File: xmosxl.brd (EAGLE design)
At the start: 130 x 85 mm, 145 parts, among them IC1 74LVC1T45W6-7, IC2 74LVC1T45W6-7, IC3 74LVC1T45W6-7, IC4 74LVC1T45W6-7, IC5 74LVC1T45W6-7, IC6 74ALVC164245DGG_11, IC7 74ALVC164245DGG_11, IC8 74LVC1T45W6-7, IC9 74LVC1T45W6-7, U1 24 MHz Osc. (F535L-24)

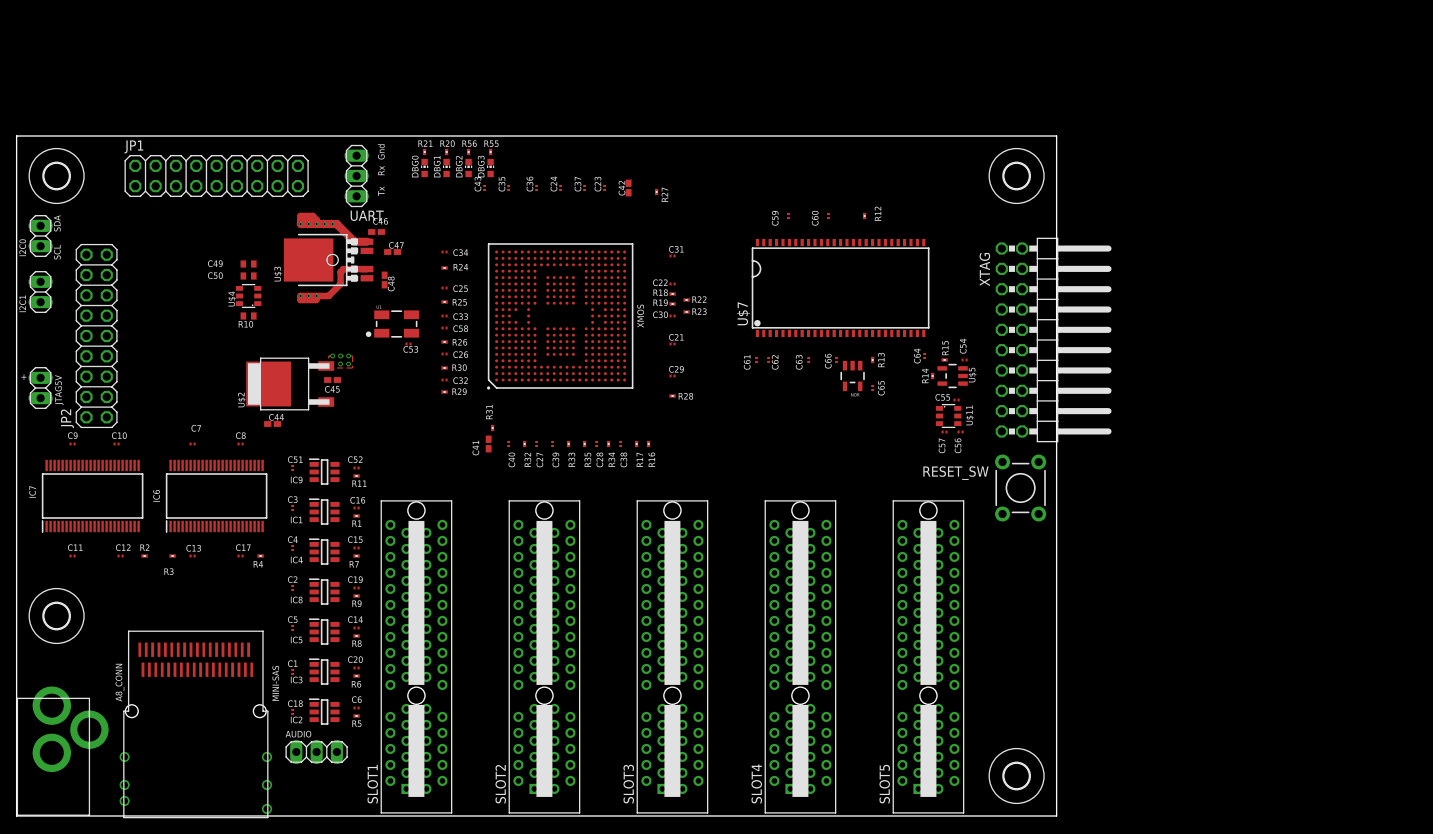
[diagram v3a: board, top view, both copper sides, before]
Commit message: Start reconfiguring for STM
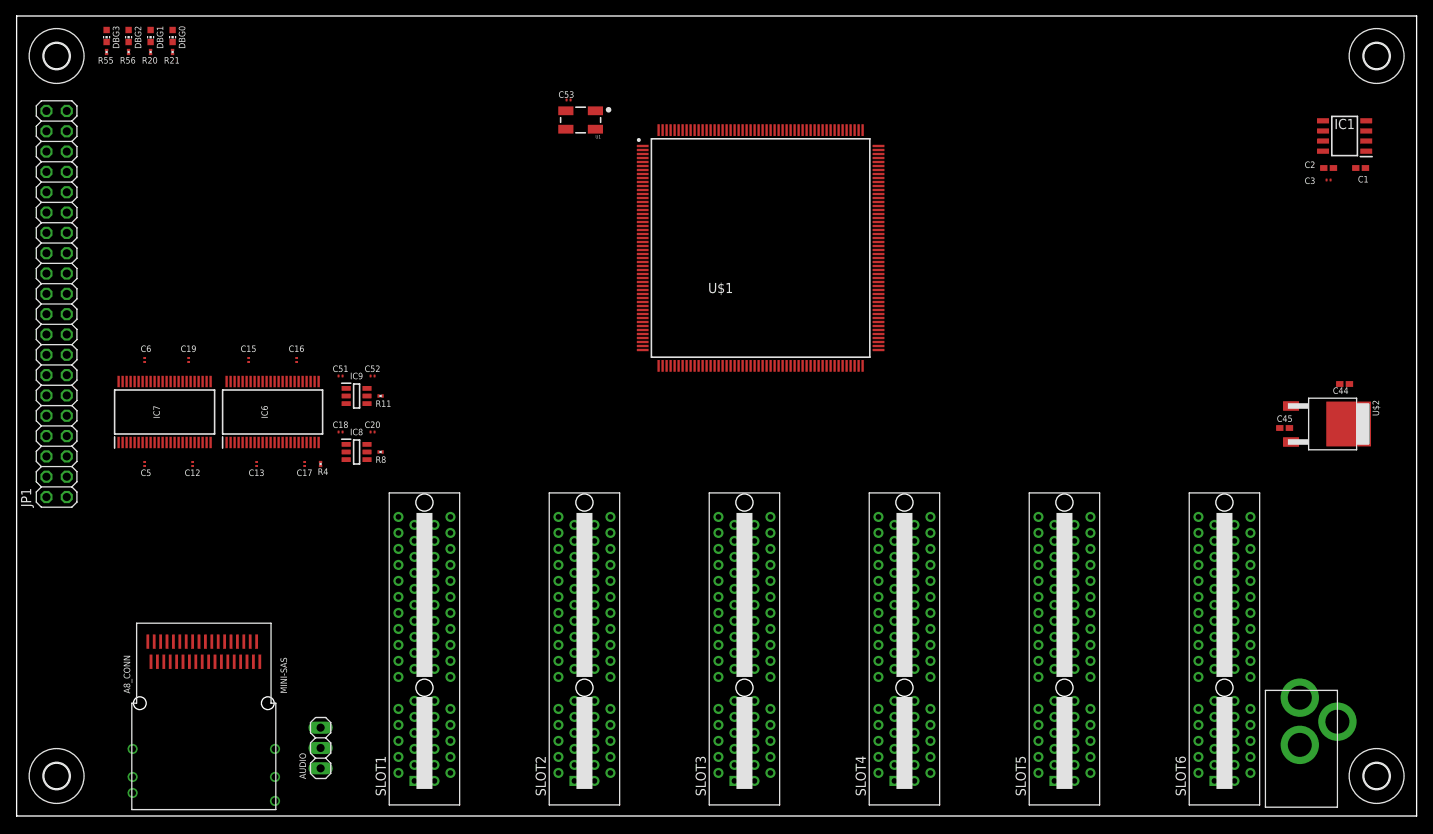
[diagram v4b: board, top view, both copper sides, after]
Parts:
- removed C10, C11, C14, C21, C22, C23, C24, C25, C26, C27, C28, C29, C30, C31, C32, C33, C34, C35, C36, C37, C38, C39, C4, C40, C43, C54, C55, C58, C7, C8, C9: 0.1uF, rcl:C0201
- removed C41, C42, C47: 10uF, rcl:C0402K
- removed C46, C48: 1uF, rcl:C0402K
- removed C49: 0.1uF, rcl:C0402
- removed C50: 120pF, rcl:C0402
- removed C56: 120pF, rcl:C0201
- removed C57: 10nF, rcl:C0201
- removed C59, C60, C61, C62, C63, C64, C65, C66: 100nF, rcl:C0201
- removed I2C0, I2C1: (no value), pinhead:1X02
- removed IC2, IC3, IC4, IC5: 74LVC1T45W6-7, samacsys:SOT95P285X140-6N
- removed JP2: (no value), pinhead:2X09
- removed JTAG5V: PSU, pinhead:1X02
- removed NOR: SN74LVC1G02, sjg-logic:SOT23-5
- removed R1, R12, R13, R18, R19, R2, R22, R23, R25, R26, R3, R5, R6, R7, R9: 10K, rcl:R0201
- removed R10: 47K, rcl:R0402
- removed R14, R15: 47K, rcl:R0201
- removed R16, R17, R31, R32, R33, R34, R35: 33R, rcl:R0201
- removed R24: 2.2R, rcl:R0201
- removed R27, R28: 43R2, rcl:R0201
- removed R29, R30: 4K7, rcl:R0201
- removed RESET_SW: MANUAL_RESET, SparkFun:TACTILE-PTH
- removed U$11: TPS3808G09DBVR, sjg-power:SOT23-6
- removed U$3: LD49300, sjg-power:TO252-51
- removed U$4: TPS3808G33DBVR, sjg-power:SOT23-6
- removed U$5: 74LVC1G07SE-7, sjg-logic:SOT23-5
- removed U$7: W9852G6KH, sjg-sdram:TSOP54-400
- removed UART: (no value), pinhead:1X03
- removed XMOS: XEF232, xmosxl:BGA374C80P21X21_1800X1800X136
- removed XTAG: 1175-1618-ND, pinhead:2X10/90
- added SLOT6: PCIE_64, pcie:PCI-E_64
- added U$1: STM32F767, xmosxl:QFP50P3000X3000X160-208N
- C1, C2: value 0.1uF -> 10uF; device rcl:C0201 -> rcl:C0402K
- C3: value 0.1uF -> 1uF
- IC1: value 74LVC1T45W6-7 -> MCP1727-1802E_SN; device samacsys:SOT95P285X140-6N -> samacsys:SOIC127P600X175-8N
- JP1: device pinhead:2X09 -> pinhead:2X20
- moved PJ-102AH 156.0 mm to (160.5, 5.50)
- moved C1 147.6 mm to (168.0, 81.0), turned to 180 degrees
- moved C2 139.7 mm to (164.0, 81.0), turned to 0 degrees
- moved IC1 135.9 mm to (166.0, 85.0), turned to 180 degrees
- moved C3 135.8 mm to (164.0, 79.5), turned to 0 degrees
- moved U$2 135.1 mm to (166.5, 49.0), turned to 270 degrees
- moved C44 134.1 mm to (166.0, 54.0), turned to 180 degrees
- moved C45 119.2 mm to (158.5, 48.5), turned to 180 degrees
- moved C6 50.9 mm to (16.0, 57.0), turned to 90 degrees
- moved DBG3 50.8 mm to (11.2, 97.5), turned to 180 degrees
- moved R55 49.6 mm to (11.2, 95.5), turned to 90 degrees
- moved H3 47.4 mm to (170.0, 95.0)
- moved DBG2 45.6 mm to (14.0, 97.5), turned to 180 degrees
- moved H4 45.0 mm to (170.0, 5.00)
- moved R56 44.3 mm to (14.0, 95.5), turned to 90 degrees
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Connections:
- removed net !DEBUG!: XMOS.D9, XTAG.11
- removed net !HALT!_DIR: IC4.5, R7.1, XMOS.C14
- removed net !IRQ!: IC3.4, XMOS.B21
- removed net !IRQ!_DIR: IC3.5, R6.1, XMOS.D14
- removed net !REF!_DIR: IC8.5, R9.1, XMOS.A15
- removed net !RESET!: R15.1, U$11.1, U$5.4, XMOS.B12, XMOS.C12
- removed net !RST!_DIR: IC2.5, R5.1, XMOS.B16
- removed net !SD_CAS!: NOR.1, U$7.17, XMOS.Y18
- removed net !SD_RAS!: U$7.18, XMOS.Y13
- removed net !SD_WE!: NOR.2, U$7.16, XMOS.AA18
- removed net A_DIR: IC7.1, IC7.24, R2.1, XMOS.B15
- removed net D_DIR: IC6.1, R3.1, XMOS.A14
- removed net EN_1V0: R10.1, U$3.1, U$4.1
- removed net JTAG_DN0: XMOS.U1, XTAG.14
- removed net JTAG_DN1: XMOS.U2, XTAG.18
- removed net JTAG_UP0: R16.2, XTAG.10
- removed net JTAG_UP1: R17.2, XTAG.6
- removed net N$1: R14.1, U$5.2, XTAG.15
- removed net N$10: R26.2, XMOS.D10
- removed net N$11: R27.2, XMOS.W16
- removed net N$12: R28.2, XMOS.W6
- removed net N$13: UART.2, XMOS.E3
- removed net N$14: NOR.4, U$7.15, U$7.39
- removed net N$15: R12.2, U$7.37
- removed net N$17: R13.2, U$7.19
- removed net N$20: UART.1, XMOS.D3
- removed net N$22: R16.1, XMOS.V2
- removed net N$23: R17.1, XMOS.V1
- removed net N$27: R31.1, XMOS.N2
- removed net N$28: R32.1, XMOS.P2
- removed net N$29: R34.1, XMOS.R1
- removed net N$30: R35.1, XMOS.R2
- removed net N$38: JTAG5V.2, XTAG.1
- removed net N$5: C50.1, U$4.4
- removed net N$6: C56.1, U$11.4
- removed net N$7: C58.1, R24.2, XMOS.F11
- removed net N$8: R14.2, U$5.5
- removed net N$9: R25.1, XMOS.C10
- removed net R/!W!_DIR: IC1.5, R1.1, XMOS.D15
- removed net RD4: IC6.35, XMOS.W18
- removed net RD5: IC6.36, XMOS.V18
- removed net RX0: JP1.1, XMOS.N1
- removed net RX1: JP1.5, XMOS.M1
- removed net RX2: JP1.9, XMOS.M2
- removed net RX3: JP1.13, XMOS.M3
- removed net RX4: JP1.17, R33.1, XMOS.L3, XMOS.P1
- removed net SBUS_A0: SLOT1.A3, SLOT2.A3, SLOT3.A3, SLOT4.A3, SLOT5.A3, XMOS.A5
- removed net SBUS_A1: SLOT1.A4, SLOT2.A4, SLOT3.A4, SLOT4.A4, SLOT5.A4, XMOS.B5
- removed net SBUS_A10: SLOT1.A13, SLOT2.A13, SLOT3.A13, SLOT4.A13, SLOT5.A13, XMOS.T1
- removed net SBUS_A11: SLOT1.A14, SLOT2.A14, SLOT3.A14, SLOT4.A14, SLOT5.A14, XMOS.U3
- removed net SBUS_A12: SLOT1.A15, SLOT2.A15, SLOT3.A15, SLOT4.A15, SLOT5.A15, XMOS.B7
- removed net SBUS_A13: SLOT1.A16, SLOT2.A16, SLOT3.A16, SLOT4.A16, SLOT5.A16, XMOS.A7
- removed net SBUS_A14: SLOT1.A17, SLOT2.A17, SLOT3.A17, SLOT4.A17, SLOT5.A17, XMOS.B6
- removed net SBUS_A15: SLOT1.A18, SLOT2.A18, SLOT3.A18, SLOT4.A18, SLOT5.A18, XMOS.C6
- removed net SBUS_A2: SLOT1.A5, SLOT2.A5, SLOT3.A5, SLOT4.A5, SLOT5.A5, XMOS.C5
- removed net SBUS_A3: SLOT1.A6, SLOT2.A6, SLOT3.A6, SLOT4.A6, SLOT5.A6, XMOS.D5
- removed net SBUS_A4: SLOT1.A7, SLOT2.A7, SLOT3.A7, SLOT4.A7, SLOT5.A7, XMOS.C4
- removed net SBUS_A5: SLOT1.A8, SLOT2.A8, SLOT3.A8, SLOT4.A8, SLOT5.A8, XMOS.D4
- removed net SBUS_A6: SLOT1.A9, SLOT2.A9, SLOT3.A9, SLOT4.A9, SLOT5.A9, XMOS.A4
- removed net SBUS_A7: SLOT1.A10, SLOT2.A10, SLOT3.A10, SLOT4.A10, SLOT5.A10, XMOS.B4
- removed net SBUS_A8: SLOT1.A11, SLOT2.A11, SLOT3.A11, SLOT4.A11, SLOT5.A11, XMOS.F1
- removed net SBUS_A9: SLOT1.A12, SLOT2.A12, SLOT3.A12, SLOT4.A12, SLOT5.A12, XMOS.R3
- removed net SBUS_CLK: SLOT1.A19, SLOT2.A19, SLOT3.A19, SLOT4.A19, SLOT5.A19, XMOS.AA8
- removed net SBUS_D0: SLOT1.A20, SLOT2.A20, SLOT3.A20, SLOT4.A20, SLOT5.A20, XMOS.G1
- removed net SBUS_D1: SLOT1.A21, SLOT2.A21, SLOT3.A21, SLOT4.A21, SLOT5.A21, XMOS.G2
- removed net SBUS_D2: SLOT1.A22, SLOT2.A22, SLOT3.A22, SLOT4.A22, SLOT5.A22, XMOS.G3
- removed net SBUS_D3: SLOT1.A23, SLOT2.A23, SLOT3.A23, SLOT4.A23, SLOT5.A23, XMOS.H2
- removed net SBUS_D4: SLOT1.A24, SLOT2.A24, SLOT3.A24, SLOT4.A24, SLOT5.A24, XMOS.H1
- removed net SBUS_D5: SLOT1.A25, SLOT2.A25, SLOT3.A25, SLOT4.A25, SLOT5.A25, XMOS.J1
- removed net SBUS_D6: SLOT1.A26, SLOT2.A26, SLOT3.A26, SLOT4.A26, SLOT5.A26, XMOS.J2
- removed net SBUS_D7: SLOT1.A27, SLOT2.A27, SLOT3.A27, SLOT4.A27, SLOT5.A27, XMOS.K3
- removed net SBUS_FLG0: SLOT1.A28, SLOT2.A28, SLOT3.A28, SLOT4.A28, SLOT5.A28, XMOS.K2
- removed net SBUS_FLG1: SLOT1.A29, SLOT2.A29, SLOT3.A29, SLOT4.A29, SLOT5.A29, XMOS.K1
- removed net SBUS_FLG2: SLOT1.A30, SLOT2.A30, SLOT3.A30, SLOT4.A30, SLOT5.A30, XMOS.V8
- removed net SBUS_FLG3: SLOT1.A31, SLOT2.A31, SLOT3.A31, SLOT4.A31, SLOT5.A31, XMOS.W8
- removed net SBUS_FLG4: SLOT1.A32, SLOT2.A32, SLOT3.A32, SLOT4.A32, SLOT5.A32, XMOS.Y8
- removed net SCL: I2C0.1, I2C1.1, R29.1, XMOS.A3
- removed net SDA: I2C0.2, I2C1.2, R30.1, XMOS.B3
- removed net SD_ADQ0: U$7.2, U$7.23, XMOS.AA13
- removed net SD_ADQ1: R19.2, U$7.24, U$7.4, XMOS.W13
- removed net SD_ADQ10: U$7.22, U$7.45, XMOS.Y17
- removed net SD_ADQ11: U$7.35, U$7.47, XMOS.AA17
- removed net SD_ADQ12: U$7.36, U$7.48, XMOS.W21
- removed net SD_ADQ13: U$7.20, U$7.50, XMOS.V20
- removed net SD_ADQ14: U$7.21, U$7.51, XMOS.V21
- removed net SD_ADQ15: U$7.53, XMOS.U20
- removed net SD_ADQ2: R22.2, U$7.25, U$7.5, XMOS.V13
- removed net SD_ADQ3: R18.2, U$7.26, U$7.7, XMOS.W14
- removed net SD_ADQ4: U$7.29, U$7.8, XMOS.V14
- removed net SD_ADQ5: U$7.10, U$7.30, XMOS.Y14
- removed net SD_ADQ6: U$7.11, U$7.31, XMOS.AA14
- removed net SD_ADQ7: R23.2, U$7.13, U$7.32, XMOS.Y12
- removed net SD_ADQ8: U$7.33, U$7.42, XMOS.V19
- removed net SD_ADQ9: U$7.34, U$7.44, XMOS.Y20
- removed net SD_CLK: U$7.38, XMOS.W12
- removed net SPI_BOPT0: SLOT1.B3, SLOT2.B3, SLOT3.B3, SLOT4.B3, SLOT5.B3, XMOS.W9
- removed net SPI_BOPT1: SLOT1.B4, SLOT2.B4, SLOT3.B4, SLOT4.B4, SLOT5.B4, XMOS.Y9
- removed net SPI_BOPT2: SLOT1.B5, SLOT2.B5, SLOT3.B5, SLOT4.B5, SLOT5.B5, XMOS.AA9
- removed net SPI_BOPT3: SLOT1.B6, SLOT2.B6, SLOT3.B6, SLOT4.B6, SLOT5.B6, XMOS.V10
- removed net SPI_BSEL0: SLOT1.B7, SLOT2.B7, SLOT3.B7, SLOT4.B7, SLOT5.B7, XMOS.V4
- removed net SPI_BSEL1: SLOT1.B8, SLOT2.B8, SLOT3.B8, SLOT4.B8, SLOT5.B8, XMOS.W4
- removed net SPI_BSEL2: SLOT1.B9, SLOT2.B9, SLOT3.B9, SLOT4.B9, SLOT5.B9, XMOS.V5
- removed net SPI_BSEL3: SLOT1.B10, SLOT2.B10, SLOT3.B10, SLOT4.B10, SLOT5.B10, XMOS.W5
- removed net SPI_CLK0: SLOT1.B11, SLOT2.B11, SLOT3.B11, SLOT4.B11, SLOT5.B11, XMOS.Y2
- removed net SPI_CLK1: XMOS.W2
- removed net SPI_IRQ0: SLOT1.B12, XMOS.B9
- removed net SPI_IRQ1: SLOT2.B12, XMOS.A9
- removed net SPI_IRQ2: SLOT3.B12, XMOS.B8
- removed net SPI_IRQ3: SLOT4.B12, XMOS.A8
- removed net SPI_IRQ4: SLOT5.B12, XMOS.C9
- removed net SPI_IRQ5: XMOS.C8
- removed net SPI_IRQ6: XMOS.D2
- removed net SPI_IRQ7: XMOS.D1
- removed net SPI_IRQ8: XMOS.E2
- removed net SPI_IRQ9: XMOS.E1
- removed net SPI_MISO0: SLOT1.B13, SLOT2.B13, SLOT3.B13, SLOT4.B13, SLOT5.B13, XMOS.V6
- removed net SPI_MISO1: XMOS.Y1
- removed net SPI_MOSI0: SLOT1.B14, SLOT2.B14, SLOT3.B14, SLOT4.B14, SLOT5.B14, XMOS.W10
- removed net SPI_MOSI1: XMOS.Y7
- removed net SPI_SS0: SLOT1.B15, XMOS.Y10
- removed net SPI_SS1: SLOT2.B15, XMOS.AA10
- removed net SPI_SS2: SLOT3.B15, XMOS.W11
- removed net SPI_SS3: SLOT4.B15, XMOS.B2
- removed net SPI_SS4: SLOT5.B15, XMOS.B1
- removed net SPI_SS5: XMOS.C2
- removed net SPI_SS6: XMOS.C1
- removed net SPI_SS7: XMOS.Y5
- removed net SPI_SS8: XMOS.AA5
- removed net SPI_SS9: XMOS.V9
- removed net TCK: XMOS.B13, XTAG.9
- removed net TDI: XMOS.A10, XTAG.5
- removed net TDO: XMOS.A13, XTAG.13
- removed net TMS: XMOS.D12, XTAG.7
- removed net TRST_N: C57.2, RESET_SW.1, RESET_SW.2, U$11.3
- removed net TX0: JP1.2, R31.2
- removed net TX1: JP1.6, R32.2
- removed net TX2: JP1.10, R33.2
- removed net TX3: JP1.14, R34.2
- removed net TX4: JP1.18, R35.2
- removed net UART_RX: XTAG.19
- removed net UART_TX: XTAG.17
- removed net XPND_CTRL0: JP2.3, XMOS.D19
- removed net XPND_CTRL1: JP2.5, XMOS.D20
- removed net XPND_CTRL2: JP2.7, XMOS.C13
- removed net XPND_CTRL3: JP2.9, XMOS.D13
- removed net XPND_CTRL4: JP2.11, XMOS.AA12
- removed net XPND_CTRL5: JP2.13, XMOS.Y15
- removed net XPND_CTRL6: JP2.15, XMOS.Y19
- removed net XPND_DATA0: JP2.2, XMOS.U21
- removed net XPND_DATA1: JP2.4, XMOS.T21
- removed net XPND_DATA2: JP2.6, XMOS.R20
- removed net XPND_DATA3: JP2.8, XMOS.R21
- removed net XPND_DATA4: JP2.10, XMOS.P20
- removed net XPND_DATA5: JP2.12, XMOS.P21
- removed net XPND_DATA6: JP2.14, XMOS.E20
- removed net XPND_DATA7: JP2.16, XMOS.E21
- new net +1.2V: C2.1, C3.1, IC1.7, IC1.8
- new net N$33: C53.1, U1.2
- new net VBAT: U$1.6
- new net VCAP: U$1.148, U$1.92
- new net VDDA: U$1.42
- new net VDDSDMMC: U$1.171
- new net VDDUSB: U$1.137
- new net VREF+: U$1.41
- new net VSS: U$1.114, U$1.125, U$1.136, U$1.14, U$1.149, U$1.170, U$1.184, U$1.202, U$1.25, U$1.51, U$1.60, U$1.72, U$1.82, U$1.93
- new net VSSA: U$1.40
- net !EXTSEL!: no longer XMOS.D21
- net !EXTSEL!_DIR: no longer XMOS.B14
- net !HALT!: now also IC6.32; no longer IC4.4, XMOS.B10
- net !HI_EXTSEL!: now also U$1.37
- net !HI_HALT!: now also IC6.17, U$1.138; no longer IC4.3
- net !HI_IRQ!: now also U$1.58; no longer IC3.3
- net !HI_MPD!: now also IC8.3, U$1.38; no longer IC5.3
- net !HI_REF!: now also IC6.13, U$1.139; no longer IC8.3
- net !HI_RST!: now also IC6.19, U$1.57; no longer IC2.3
- net !MPD!: now also IC8.4; no longer IC5.4, XMOS.C20
- net !MPD!_DIR: now also IC8.5; no longer IC5.5, XMOS.AA19
- net !REF!: now also IC6.36; no longer IC8.4, XMOS.V12
- net !RST!: now also IC6.30; no longer IC2.4, XMOS.C21
- net +3V3: no longer C10.1, C14.1, C21.1, C22.1, C23.1, C24.1, C25.1, C26.1, C27.1, C28.1, C41.1, C43.1, C49.1, C54.1, C55.1, C59.1, C60.1, C61.1, C62.1, C63.1, C64.1, C65.1, C66.1, C7.1, C8.1, C9.1, IC1.6, IC2.6, IC3.6, IC4.6, IC5.6, NOR.5, R1.2, R10.2, R11.1, R12.1, R15.2, R18.1, R25.2, R29.2, R30.2, R5.2, R6.2, R7.2, R8.2, R9.2, SLOT1.B16, SLOT2.B17, SLOT3.B16, SLOT3.B17, SLOT4.B18, SLOT5.B16, SLOT5.B18, U$11.6, U$4.5, U$4.6, U$7.1, U$7.14, U$7.27, U$7.3, U$7.43, U$7.49, U$7.9, XMOS.A11, XMOS.A16, XMOS.A2, XMOS.A20, XMOS.A6, XMOS.AA11, XMOS.AA2, XMOS.AA20, XMOS.C11, XMOS.D7, XMOS.E15, XMOS.E7, XMOS.F2, XMOS.F20, XMOS.L1, XMOS.L21, XMOS.T2, XMOS.T20, XMOS.U11, XMOS.U15, XMOS.U7
- net +5V: now also IC1.2, IC1.3, SLOT6.A1, SLOT6.A2, SLOT6.B1, SLOT6.B2; no longer C11.1, C2.1, C3.1, C4.1, C46.1, C48.1, IC2.1, IC3.1, IC4.1, IC5.1, JP1.3, JP1.4, JP1.7, JP1.8, JP2.1, JTAG5V.1, U$3.2, U$3.5
- net A0: no longer XMOS.R19
- net A1: no longer XMOS.N20
- net A10: no longer XMOS.J21
- net A11: no longer XMOS.J20
- net A12: no longer XMOS.H20
- net A13: no longer XMOS.H21
- net A14: no longer XMOS.G21
- net A15: no longer XMOS.G20
- net A2: no longer XMOS.N21
- net A3: no longer XMOS.M21
- net A4: no longer XMOS.M20
- net A5: no longer XMOS.M19
- net A6: no longer XMOS.L19
- net A7: no longer XMOS.K19
- net A8: no longer XMOS.K20
- net A9: no longer XMOS.K21
- net CLK: no longer XMOS.Y21
- net CTRL_DIR: now also IC6.1, IC7.1, IC7.24
- net D0: no longer XMOS.B20
- net D1: no longer XMOS.B19
- net D2: no longer XMOS.B18
- net D3: no longer XMOS.A18
- net D4: no longer XMOS.B17
- net D5: no longer XMOS.A17
- net D6: no longer XMOS.A19
- net D7: no longer XMOS.C18
- net GND: now also IC1.4, R11.1, R8.2; no longer C10.2, C11.2, C14.2, C21.2, C22.2, C23.2, C24.2, C25.2, C26.2, C27.2, C28.2, C29.2, C30.2, C31.2, C32.2, C33.2, C34.2, C35.2, C36.2, C37.2, C38.2, C39.2, C4.2, C40.2, C41.2, C42.2, C43.2, C46.2, C47.2, C48.2, C49.2, C50.2, C53.1, C54.2, C55.2, C56.2, C57.1, C58.2, C59.2, C60.2, C61.2, C62.2, C63.2, C64.2, C65.2, C66.2, C7.2, C8.2, C9.2, IC1.2, IC2.2, IC3.2, IC4.2, IC5.2, IC6.17, IC6.19, IC6.30, IC6.32, JP1.11, JP1.12, JP1.15, JP1.16, JP2.17, JP2.18, NOR.3, R13.1, R19.1, R2.2, R22.1, R23.1, R26.1, R27.1, R28.1, R3.2, RESET_SW.3, RESET_SW.4, SLOT1.B17, SLOT1.B18, SLOT1.B19, SLOT1.B20, SLOT1.B21, SLOT1.B22, SLOT1.B23, SLOT1.B24, SLOT1.B25, SLOT1.B26, SLOT1.B27, SLOT1.B28, SLOT1.B29, SLOT1.B30, SLOT1.B31, SLOT1.B32, SLOT2.B16, SLOT2.B18, SLOT2.B19, SLOT2.B20, SLOT2.B21, SLOT2.B22, SLOT2.B23, SLOT2.B24, SLOT2.B25, SLOT2.B26, SLOT2.B27, SLOT2.B28, SLOT2.B29, SLOT2.B30, SLOT2.B31, SLOT2.B32, SLOT3.B18, SLOT3.B19, SLOT3.B20, SLOT3.B21, SLOT3.B22, SLOT3.B23, SLOT3.B24, SLOT3.B25, SLOT3.B26, SLOT3.B27, SLOT3.B28, SLOT3.B29, SLOT3.B30, SLOT3.B31, SLOT3.B32, SLOT4.B16, SLOT4.B17, SLOT4.B19, SLOT4.B20, SLOT4.B21, SLOT4.B22, SLOT4.B23, SLOT4.B24, SLOT4.B25, SLOT4.B26, SLOT4.B27, SLOT4.B28, SLOT4.B29, SLOT4.B30, SLOT4.B31, SLOT4.B32, SLOT5.B17, SLOT5.B19, SLOT5.B20, SLOT5.B21, SLOT5.B22, SLOT5.B23, SLOT5.B24, SLOT5.B25, SLOT5.B26, SLOT5.B27, SLOT5.B28, SLOT5.B29, SLOT5.B30, SLOT5.B31, SLOT5.B32, U$11.2, U$3.TAB, U$4.2, U$5.3, U$7.12, U$7.28, U$7.41, U$7.46, U$7.52, U$7.54, U$7.6, U1.2, UART.3, XMOS.A1, XMOS.A21, XMOS.AA1, XMOS.AA21, XMOS.B11, XMOS.C15, XMOS.C7, XMOS.D18, XMOS.D6, XMOS.E16, XMOS.E19, XMOS.E6, XMOS.F10, XMOS.F19, XMOS.F21, XMOS.F3, XMOS.G19, XMOS.J13, XMOS.J14, XMOS.J15, XMOS.J16, XMOS.J17, XMOS.J5, XMOS.J6, XMOS.J7, XMOS.J8, XMOS.J9, XMOS.K13, XMOS.K14, XMOS.K15, XMOS.K16, XMOS.K17, XMOS.K5, XMOS.K6, XMOS.K7, XMOS.K8, XMOS.K9, XMOS.L13, XMOS.L14, XMOS.L15, XMOS.L16, XMOS.L17, XMOS.L2, XMOS.L20, XMOS.L5, XMOS.L6, XMOS.L7, XMOS.L8, XMOS.L9, XMOS.M13, XMOS.M14, XMOS.M15, XMOS.M16, XMOS.M17, XMOS.M5, XMOS.M6, XMOS.M7, XMOS.M8, XMOS.M9, XMOS.N13, XMOS.N14, XMOS.N15, XMOS.N16, XMOS.N17, XMOS.N5, XMOS.N6, XMOS.N7, XMOS.N8, XMOS.N9, XMOS.T11, XMOS.T19, XMOS.T3, XMOS.U16, XMOS.U6, XMOS.V17, XMOS.W15, XMOS.W17, XMOS.W7, XMOS.Y11, XTAG.12, XTAG.16, XTAG.20, XTAG.4, XTAG.8
- net HI_A0: now also U$1.61
- net HI_A1: now also U$1.62
- net HI_A10: now also U$1.90
- net HI_A11: now also U$1.91
- net HI_A12: now also U$1.104
- net HI_A13: now also U$1.105
- net HI_A14: now also U$1.106
- net HI_A15: now also U$1.107
- net HI_A2: now also U$1.63
- net HI_A3: now also U$1.192
- net HI_A4: now also U$1.193
- net HI_A5: now also U$1.194
- net HI_A6: now also U$1.195
- net HI_A7: now also U$1.196
- net HI_A8: now also U$1.198
- net HI_A9: now also U$1.199
- net HI_CLK: now also U$1.35
- net HI_D0: now also U$1.126
- net HI_D1: now also U$1.127
- net HI_D2: now also U$1.128
- net HI_D3: now also U$1.186
- net HI_D4: now also U$1.187
- net HI_D5: now also U$1.188
- net HI_D6: now also U$1.189
- net HI_D7: now also U$1.190
- net HI_R/!W!: now also IC6.14, U$1.36; no longer IC1.3
- net HI_RD4: now also U$1.140; no longer IC6.14
- net HI_RD5: now also U$1.141; no longer IC6.13
- net N$2: no longer XMOS.A12
- net N$4: no longer XMOS.C16
- net N$56: no longer XMOS.D16
- net N$57: no longer XMOS.C17
- net N$63: no longer XMOS.D17
- net R/!W!: now also IC6.35; no longer IC1.4, XMOS.W20
- net VDD: now also U$1.103, U$1.115, U$1.124, U$1.15, U$1.150, U$1.158, U$1.185, U$1.204, U$1.26, U$1.39, U$1.52, U$1.59, U$1.73, U$1.83, U$1.94; no longer C29.1, C30.1, C31.1, C32.1, C33.1, C34.1, C35.1, C36.1, C37.1, C38.1, C39.1, C40.1, C42.1, C47.1, R24.1, U$11.5, U$3.4, XMOS.C19, XMOS.C3, XMOS.E13, XMOS.E14, XMOS.E17, XMOS.E18, XMOS.E4, XMOS.E5, XMOS.E8, XMOS.E9, XMOS.F12, XMOS.F13, XMOS.F14, XMOS.F15, XMOS.F16, XMOS.F17, XMOS.F18, XMOS.F4, XMOS.F5, XMOS.F6, XMOS.F7, XMOS.F8, XMOS.F9, XMOS.H19, XMOS.H3, XMOS.J19, XMOS.J3, XMOS.N19, XMOS.N3, XMOS.P19, XMOS.P3, XMOS.T10, XMOS.T12, XMOS.T13, XMOS.T14, XMOS.T16, XMOS.T17, XMOS.T18, XMOS.T4, XMOS.T5, XMOS.T6, XMOS.T8, XMOS.T9, XMOS.U13, XMOS.U14, XMOS.U17, XMOS.U18, XMOS.U4, XMOS.U5, XMOS.U9
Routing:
- net +5V: track 27.7 -> 0.00 mm, vias 8 -> 0
- removed copper zone on layer 1, net +3V3
- removed copper zone on layer 15, net +3V3
- removed copper zone on layer 15, net +5V
- removed copper zone on layer 3, net VDD
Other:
- board size 130 x 85 mm -> 175 x 100 mm
- board text removed: "+"
- board text removed: "Gnd"
- board text removed: "Rx"
- board text removed: "SCL"
- board text removed: "SDA"
- board text removed: "Tx"

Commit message: Add the FPGA
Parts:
- added IC2: ICE40HX4K-TQ144, samacsys:QFP50P2200X2200X160-144N
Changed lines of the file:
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@@
 <attribute name="VALUE" x="163.365" y="77.595" size="1.27" layer="27"/>
+</element>
+<element name="IC2" library="samacsys" package="QFP50P2200X2200X160-144N" value="ICE40HX4K-TQ144" x="29" y="76" smashed="yes">
+<attribute name="ARROW_PART_NUMBER" value="ICE40HX4K-TQ144" x="29" y="76" size="1.778" layer="27" display="off"/>
+<attribute name="ARROW_PRICE-STOCK" value="https://www.arrow.com/en/products/ice40hx4k-tq144/lattice-semiconductor" x="29" y="76" size="1.778" layer="27" display="off"/>
+<attribute name="DESCRIPTION" value="FPGA - Field Programmable Gate Array" x="29" y="76" size="1.778" layer="27" display="off"/>
+<attribute name="HEIGHT" value="1.6mm" x="29" y="76" size="1.778" layer="27" display="off"/>
+<attribute name="MANUFACTURER_NAME" value="Lattice Semiconductor" x="29" y="76" size="1.778" layer="27" display="off"/>
+<attribute name="MANUFACTURER_PART_NUMBER" value="iCE40HX4K-TQ144" x="29" y="76" size="1.778" layer="27" display="off"/>
+<attribute name="MOUSER_PART_NUMBER" value="842-ICE40HX4K-TQ144" x="29" y="76" size="1.778" layer="27" display="off"/>
+<attribute name="MOUSER_PRICE-STOCK" value="https://www.mouser.co.uk/ProductDetail/Lattice/iCE40HX4K-TQ144?qs=F9A14TELRMvGNTZXkNDuOw%3D%3D" x="29" y="76" size="1.778" layer="27" display="off"/>
+<attribute name="NAME" x="29" y="73" size="1.27" layer="25" align="center"/>
+<attribute name="VALUE" x="29" y="76" size="1.27" layer="27" align="center"/>
 </element>
 </elements>

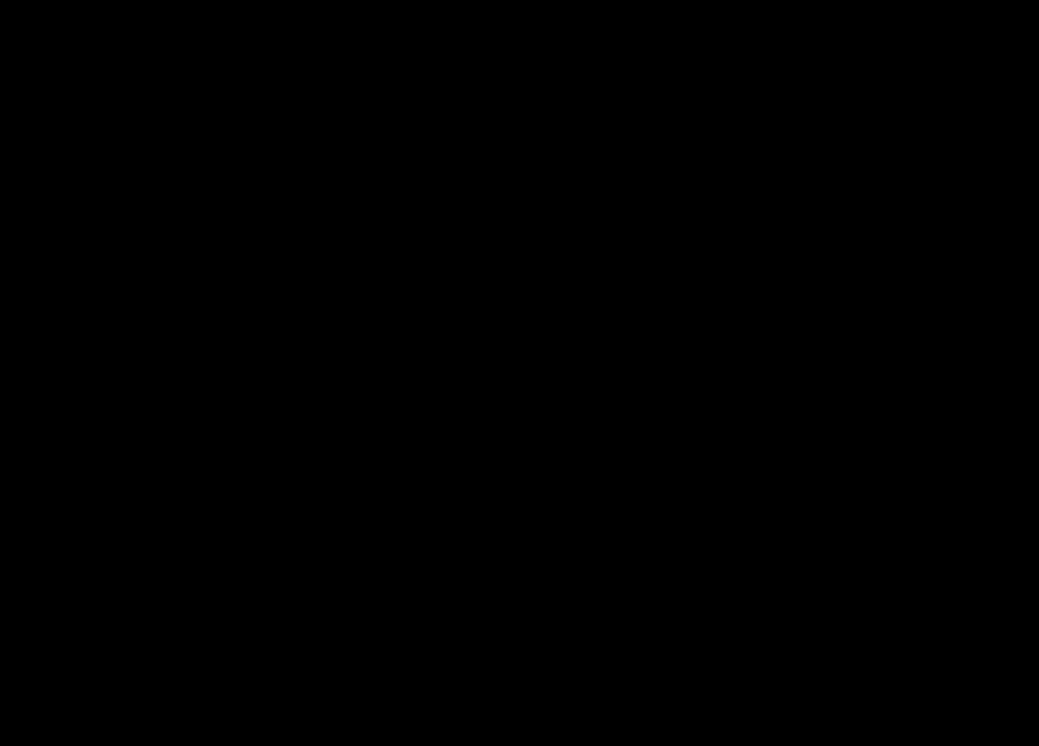
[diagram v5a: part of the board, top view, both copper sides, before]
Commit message: Add the DRAM chip. We now have basically all the major parts on the board. Plenty of space :)
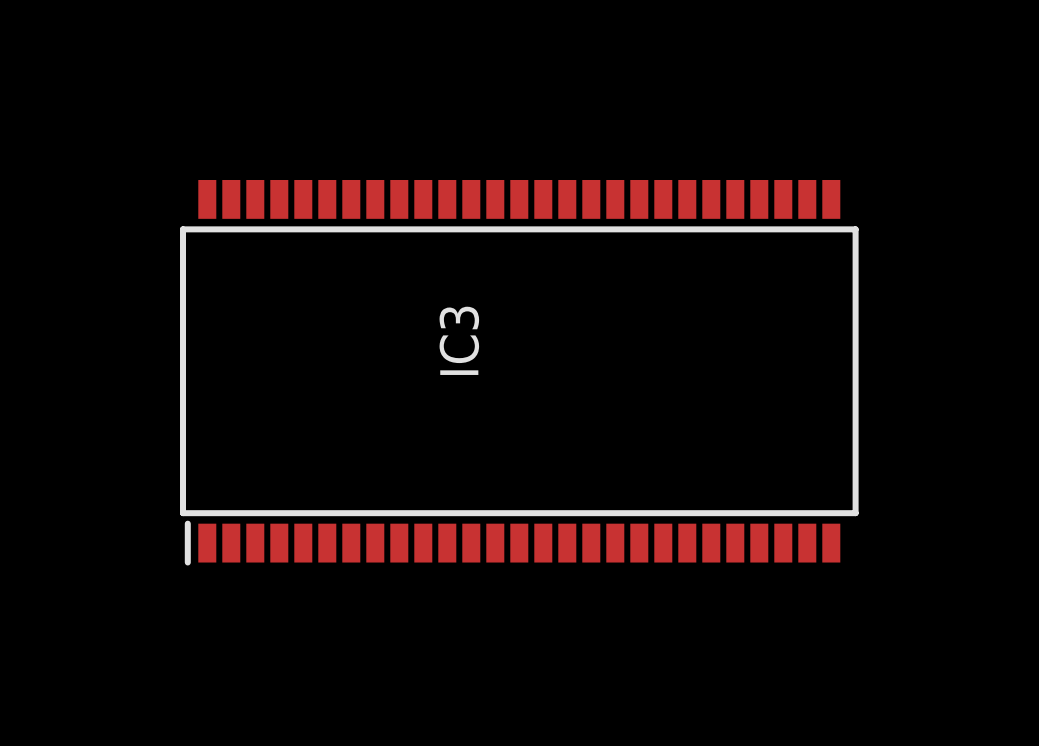
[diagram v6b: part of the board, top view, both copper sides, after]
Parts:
- added IC3: AS4C32M8SA-6TIN, samacsys:SOP80P1176X120-54N
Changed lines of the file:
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@@
 <attribute name="VALUE" x="29" y="76" size="1.27" layer="27" align="center"/>
+</element>
+<element name="IC3" library="samacsys" package="SOP80P1176X120-54N" value="AS4C32M8SA-6TIN" x="134" y="71" smashed="yes" rot="R90">
+<attribute name="ARROW_PART_NUMBER" value="MT48LC32M8A2P-6AG" x="134" y="71" size="1.778" layer="27" rot="R90" display="off"/>
+<attribute name="ARROW_PRICE-STOCK" value="https://www.arrow.com/en/products/mt48lc32m8a2p-6ag/micron-technology" x="134" y="71" size="1.778" layer="27" rot="R90" display="off"/>
+<attribute name="DESCRIPTION" value="DRAM Chip SDRAM 256Mbit 32Mx8 3.3V 54-Pin TSOP-II" x="134" y="71" size="1.778" layer="27" rot="R90" display="off"/>
+<attribute name="HEIGHT" value="1.2mm" x="134" y="71" size="1.778" layer="27" rot="R90" display="off"/>
+<attribute name="MANUFACTURER_NAME" value="Micron" x="134" y="71" size="1.778" layer="27" rot="R90" display="off"/>
+<attribute name="MANUFACTURER_PART_NUMBER" value="MT48LC32M8A2P-6AG" x="134" y="71" size="1.778" layer="27" rot="R90" display="off"/>
+<attribute name="MOUSER_PART_NUMBER" value="" x="134" y="71" size="1.778" layer="27" rot="R90" display="off"/>
+<attribute name="MOUSER_PRICE-STOCK" value="" x="134" y="71" size="1.778" layer="27" rot="R90" display="off"/>
+<attribute name="NAME" x="132" y="72" size="1.27" layer="25" rot="R90" align="center"/>
+<attribute name="VALUE" x="134" y="71" size="1.27" layer="27" rot="R90" align="center"/>
 </element>
 </elements>
